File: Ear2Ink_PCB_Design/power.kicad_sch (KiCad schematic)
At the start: 20 parts, among them P1 OSTTE020104, U2 TPS562208DDCR, U3 AZ1117-3.3, U4 LM66100DCK, U5 LM66100DCK

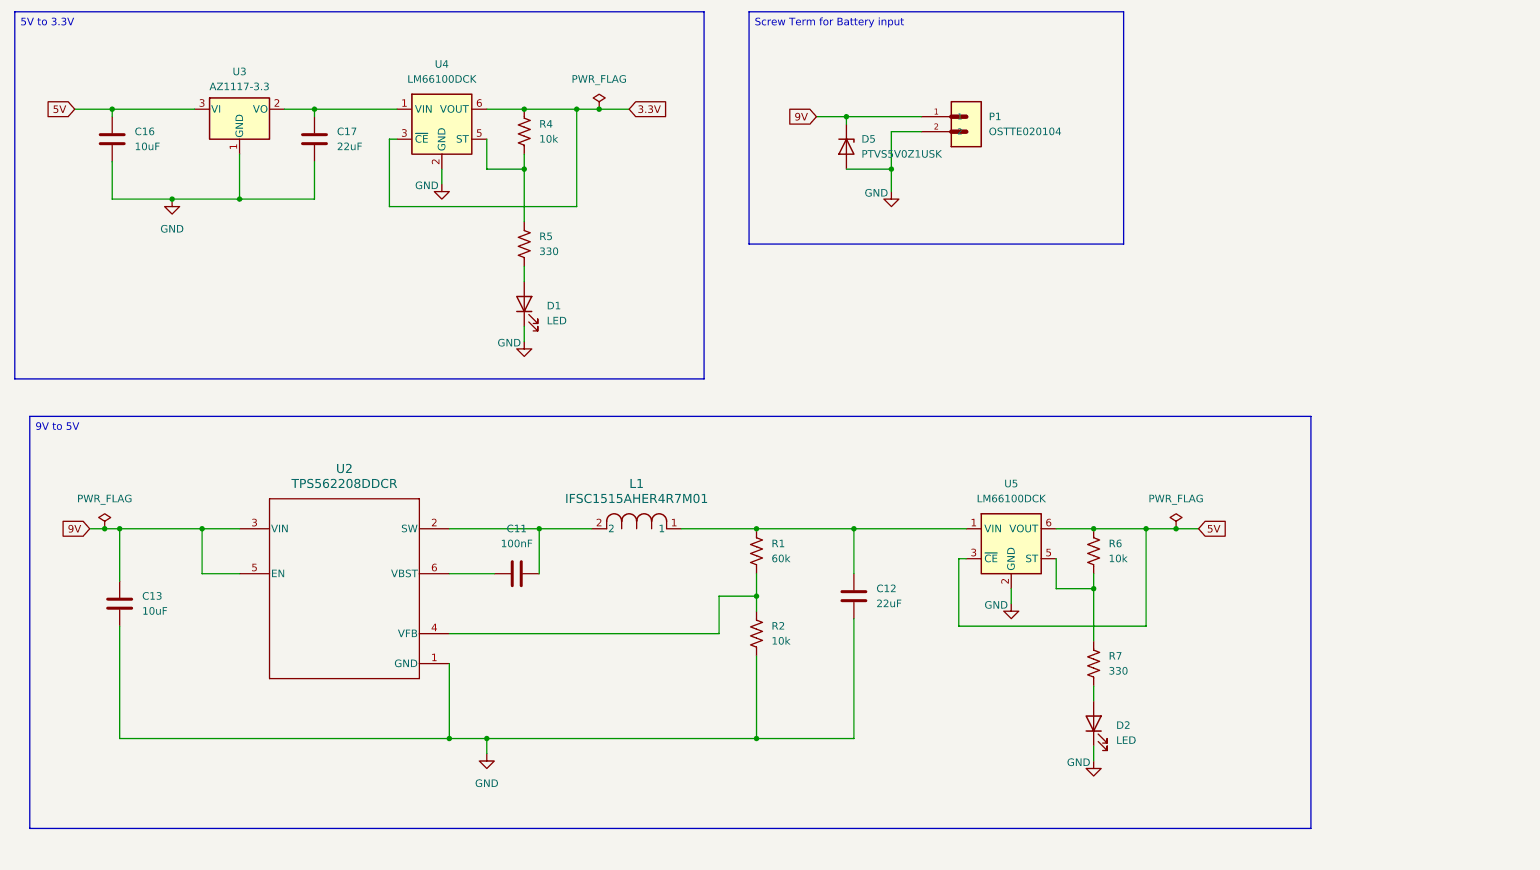
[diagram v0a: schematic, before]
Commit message: added current monitor
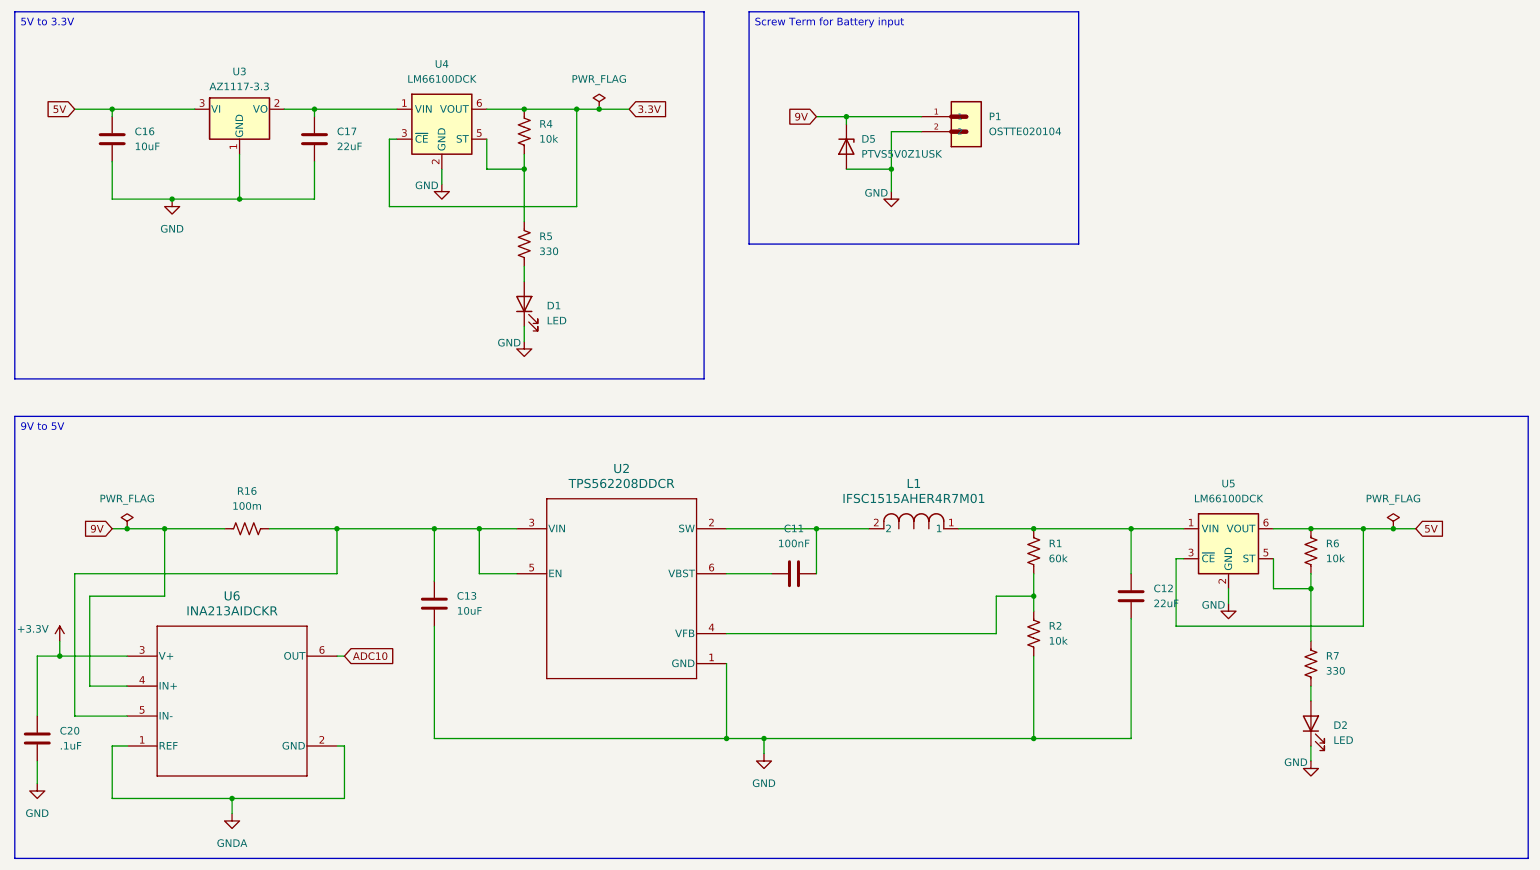
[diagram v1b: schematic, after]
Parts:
- added C20: .1uF, Capacitor_SMD:C_0603_1608Metric_Pad1.08x0.95mm_HandSolder, symbol Device:C
- added R16: 100m, Resistor_SMD:R_0603_1608Metric_Pad0.98x0.95mm_HandSolder, symbol Device:R_US
- added U6: INA213AIDCKR, Current_Monitor:DCK0006A_N, symbol Current_Monitor:INA213AIDCKR
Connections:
- net 9V: now also R16.2, U6.4 (IN+); no longer C13.2, U2.3 (VIN), U2.5 (EN)
- net GND: now also C20.1
- new net: C13.2, R16.1, U2.3 (VIN), U2.5 (EN), U6.5 (IN-)
- new net +3.3V: C20.2, U6.3 (V+)
- new net ADC10: U6.6 (OUT)
- new net GNDA: U6.1 (REF), U6.2 (GND)
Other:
- moved on the sheet: C11, C12, C13, D2, L1, R1, R2, R6, R7, U2, U5

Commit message: working on erc errors
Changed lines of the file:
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@@
 	)
 	(global_label "9V"
-		(shape input)
+		(shape output)
 		(at 158.75 40.64 180)
 		(fields_autoplaced yes)
@@
 	)
 	(global_label "5V"
-		(shape input)
+		(shape output)
 		(at 260.35 110.49 0)
 		(fields_autoplaced yes)
@@
 	)
 	(global_label "3.3V"
-		(shape input)
+		(shape output)
 		(at 127 39.37 0)
 		(fields_autoplaced yes)

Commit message: fixed erc stuff
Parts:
- added NT1: NetTie_2, NetTie:NetTie-2_SMD_Pad0.5mm, symbol Device:NetTie_2
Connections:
- net 3.3V is gone; now on net +3.3V: R4.1, U4.3 (~{CE}), U4.6 (VOUT)
- net GND: now also NT1.2
- net GNDA: now also NT1.1
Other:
- moved on the sheet: C11, R1

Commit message: SDIO to SPI
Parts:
- D1, D2: footprint Resistor_SMD:R_0805_2012Metric_Pad1.20x1.40mm_HandSolder -> LED_SMD:LED_0805_2012Metric_Pad1.15x1.40mm_HandSolder
- R1, R2, R4, R5, R6, R7: footprint Capacitor_SMD:C_0603_1608Metric_Pad1.08x0.95mm_HandSolder -> Resistor_SMD:R_0603_1608Metric_Pad0.98x0.95mm_HandSolder
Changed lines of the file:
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@@
 			)
 		)
-		(property "Footprint" "Capacitor_SMD:C_0603_1608Metric_Pad1.08x0.95mm_HandSolder"
+		(property "Footprint" "Resistor_SMD:R_0603_1608Metric_Pad0.98x0.95mm_HandSolder"
 			(at 243.586 114.554 90)
 			(effects
@@
 			)
 		)
-		(property "Footprint" "Capacitor_SMD:C_0603_1608Metric_Pad1.08x0.95mm_HandSolder"
+		(property "Footprint" "Resistor_SMD:R_0603_1608Metric_Pad0.98x0.95mm_HandSolder"
 			(at 196.596 115.824 90)
 			(effects
@@
 			)
 		)
-		(property "Footprint" "Capacitor_SMD:C_0603_1608Metric_Pad1.08x0.95mm_HandSolder"
+		(property "Footprint" "Resistor_SMD:R_0603_1608Metric_Pad0.98x0.95mm_HandSolder"
 			(at 243.586 133.604 90)
 			(effects
@@
 			)
 		)
-		(property "Footprint" "Resistor_SMD:R_0805_2012Metric_Pad1.20x1.40mm_HandSolder"
+		(property "Footprint" "LED_SMD:LED_0805_2012Metric_Pad1.15x1.40mm_HandSolder"
 			(at 109.22 72.39 0)
 			(effects
@@
 			)
 		)
-		(property "Footprint" "Capacitor_SMD:C_0603_1608Metric_Pad1.08x0.95mm_HandSolder"
+		(property "Footprint" "Resistor_SMD:R_0603_1608Metric_Pad0.98x0.95mm_HandSolder"
 			(at 110.236 43.434 90)
 			(effects
@@
 			)
 		)
-		(property "Footprint" "Resistor_SMD:R_0805_2012Metric_Pad1.20x1.40mm_HandSolder"
+		(property "Footprint" "LED_SMD:LED_0805_2012Metric_Pad1.15x1.40mm_HandSolder"
 			(at 242.57 143.51 0)
 			(effects
@@
 			)
 		)
-		(property "Footprint" "Capacitor_SMD:C_0603_1608Metric_Pad1.08x0.95mm_HandSolder"
+		(property "Footprint" "Resistor_SMD:R_0603_1608Metric_Pad0.98x0.95mm_HandSolder"
 			(at 196.596 128.524 90)
 			(effects
@@
 			)
 		)
-		(property "Footprint" "Capacitor_SMD:C_0603_1608Metric_Pad1.08x0.95mm_HandSolder"
+		(property "Footprint" "Resistor_SMD:R_0603_1608Metric_Pad0.98x0.95mm_HandSolder"
 			(at 110.236 62.484 90)
 			(effects

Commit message: resistors changed UPDATE LAYOUT
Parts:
- R5: value 330 -> 220
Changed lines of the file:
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@@
 			)
 		)
-		(property "Value" "330"
+		(property "Value" "220"
 			(at 111.76 63.4999 0)
 			(effects

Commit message: New Parts Added
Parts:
- L1: value IFSC1515AHER4R7M01 -> 47uH
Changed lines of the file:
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@@
 			)
 		)
-		(property "Value" "IFSC1515AHER4R7M01"
+		(property "Value" "47uH"
 			(at 175.26 105.41 0)
 			(effects

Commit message: Did a lot of stuff
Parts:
- added JP1: SolderJumper_2_Open, Jumper:SolderJumper-2_P1.3mm_Open_Pad1.0x1.5mm, symbol Jumper:SolderJumper_2_Open
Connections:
- net 9V: now also JP1.1 (A)
- net GND: now also U6.2 (GND)
- net GNDA: no longer U6.2 (GND)
- net Buck_In: now reaches C13.2, R16.1, U2.3 (VIN), U2.5 (EN), U6.5 (IN-)
- net Buck_In: now also JP1.2 (B)
- net 5V_Out: now reaches C12.1, L1.1, R1.1, U5.1 (VIN)
- net LDO_Out: now reaches C17.1, U3.2 (VO), U4.1 (VIN)
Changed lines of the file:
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@@
 	)
 	(junction
-		(at 59.69 156.21)
+		(at 53.34 110.49)
 		(diameter 0)
 		(color 0 0 0 0)
@@
 	)
 	(junction
+		(at 39.37 156.21)
+		(diameter 0)
+		(color 0 0 0 0)
+	)
+	(junction
+		(at 69.85 110.49)
+		(diameter 0)
+		(color 0 0 0 0)
+	)
+	(junction
 		(at 30.48 132.08)
 		(diameter 0)
@@
 	)
 	(junction
-		(at 50.8 156.21)
-		(diameter 0)
-		(color 0 0 0 0)
-	)
-	(junction
 		(at 154.94 110.49)
 		(diameter 0)
@@
 	(wire
 		(pts
+			(xy 58.42 100.33) (xy 53.34 100.33)
+		)
+		(stroke
+			(width 0)
+			(type default)
+		)
+	)
+	(wire
+		(pts
 			(xy 41.91 137.16) (xy 35.56 137.16)
 		)
@@
 	(wire
 		(pts
-			(xy 50.8 156.21) (xy 59.69 156.21)
-		)
-		(stroke
-			(width 0)
-			(type default)
-		)
-	)
-	(wire
-		(pts
 			(xy 189.23 128.27) (xy 189.23 121.92)
 		)
@@
 	(wire
 		(pts
-			(xy 39.37 156.21) (xy 50.8 156.21)
-		)
-		(stroke
-			(width 0)
-			(type default)
-		)
-	)
-	(wire
-		(pts
 			(xy 195.58 132.08) (xy 195.58 146.05)
 		)
@@
 	(wire
 		(pts
+			(xy 39.37 156.21) (xy 50.8 156.21)
+		)
+		(stroke
+			(width 0)
+			(type default)
+		)
+	)
+	(wire
+		(pts
 			(xy 73.66 39.37) (xy 87.63 39.37)
 		)
@@
 	(wire
 		(pts
+			(xy 69.85 110.49) (xy 73.66 110.49)
+		)
+		(stroke
+			(width 0)
+			(type default)
+		)
+	)
+	(wire
+		(pts
+			(xy 53.34 110.49) (xy 58.42 110.49)
+		)
+		(stroke
+			(width 0)
+			(type default)
+		)
+	)
+	(wire
+		(pts
 			(xy 242.57 120.65) (xy 236.22 120.65)
 		)
@@
 	(wire
 		(pts
-			(xy 66.04 110.49) (xy 73.66 110.49)
+			(xy 66.04 110.49) (xy 69.85 110.49)
 		)
 		(stroke
@@
 	(wire
 		(pts
+			(xy 69.85 100.33) (xy 69.85 110.49)
+		)
+		(stroke
+			(width 0)
+			(type default)
+		)
+	)
+	(wire
+		(pts
 			(xy 143.51 146.05) (xy 149.86 146.05)
 		)
@@
 	(wire
 		(pts
-			(xy 48.26 110.49) (xy 58.42 110.49)
+			(xy 48.26 110.49) (xy 53.34 110.49)
 		)
 		(stroke
@@
 	(wire
 		(pts
-			(xy 59.69 156.21) (xy 78.74 156.21)
+			(xy 236.22 120.65) (xy 236.22 115.57)
 		)
 		(stroke
@@
 	(wire
 		(pts
-			(xy 236.22 120.65) (xy 236.22 115.57)
+			(xy 39.37 39.37) (xy 53.34 39.37)
 		)
 		(stroke
@@
 	(wire
 		(pts
-			(xy 39.37 39.37) (xy 53.34 39.37)
+			(xy 53.34 100.33) (xy 53.34 110.49)
 		)
 		(stroke
@@
 	(wire
 		(pts
-			(xy 59.69 156.21) (xy 59.69 158.75)
+			(xy 39.37 156.21) (xy 39.37 158.75)
 		)
 		(stroke
@@
 	(wire
 		(pts
+			(xy 66.04 100.33) (xy 69.85 100.33)
+		)
+		(stroke
+			(width 0)
+			(type default)
+		)
+	)
+	(wire
+		(pts
 			(xy 242.57 120.65) (xy 242.57 129.54)
 		)
@@
 		)
 	)
+	(label "LDO_Out"
+		(at 76.2 39.37 0)
+		(effects
+			(font
+				(size 1.27 1.27)
+			)
+			(justify left bottom)
+		)
+	)
+	(label "5V_Out"
+		(at 186.69 110.49 0)
+		(effects
+			(font
+				(size 1.27 1.27)
+			)
+			(justify left bottom)
+		)
+	)
+	(label "Buck_In"
+		(at 86.36 110.49 0)
+		(effects
+			(font
+				(size 1.27 1.27)
+			)
+			(justify left bottom)
+		)
+	)
 	(global_label "9V"
 		(shape input)
@@
 	(symbol
 		(lib_id "power:GNDA")
-		(at 59.69 158.75 0)
+		(at 39.37 158.75 0)
 		(unit 1)
 		(exclude_from_sim no)
@@
 		(fields_autoplaced yes)
 		(property "Reference" "#PWR034"
-			(at 59.69 165.1 0)
+			(at 39.37 165.1 0)
 			(effects
 				(font
@@
 		)
 		(property "Value" "GNDA"
-			(at 59.69 163.83 0)
+			(at 39.37 163.83 0)
 			(effects
 				(font
@@
 		)
 		(property "Footprint" ""
-			(at 59.69 158.75 0)
+			(at 39.37 158.75 0)
 			(effects
 				(font
@@
 		)
 		(property "Datasheet" ""
-			(at 59.69 158.75 0)
+			(at 39.37 158.75 0)
 			(effects
 				(font
@@
 		)
 		(property "Description" "Power symbol creates a global label with name \"GNDA\" , analog ground"
-			(at 59.69 158.75 0)
+			(at 39.37 158.75 0)
 			(effects
 				(font
@@
 	)
 	(symbol
+		(lib_id "power:GND")
+		(at 78.74 156.21 0)
+		(unit 1)
+		(exclude_from_sim no)
+		(in_bom yes)
+		(on_board yes)
+		(dnp no)
+		(fields_autoplaced yes)
+		(property "Reference" "#PWR048"
+			(at 78.74 162.56 0)
+			(effects
+				(font
+					(size 1.27 1.27)
+				)
+				(hide yes)
+			)
+		)
+		(property "Value" "GND"
+			(at 78.74 161.29 0)
+			(effects
+				(font
+					(size 1.27 1.27)
+				)
+			)
+		)
+		(property "Footprint" ""
+			(at 78.74 156.21 0)
+			(effects
+				(font
+					(size 1.27 1.27)
+				)
+				(hide yes)
+			)
+		)
+		(property "Datasheet" ""
+			(at 78.74 156.21 0)
+			(effects
+				(font
+					(size 1.27 1.27)
+				)
+				(hide yes)
+			)
+		)
+		(property "Description" "Power symbol creates a global label with name \"GND\" , ground"
+			(at 78.74 156.21 0)
+			(effects
+				(font
+					(size 1.27 1.27)
+				)
+				(hide yes)
+			)
+		)
+		(pin "1"
+		)
+		(instances
+			(project "Ear2Ink_PCB_Design"
+				(path "/cdb6d8ac-bdfd-4608-bf70-aa82e76498ad/f1b1c289-1e04-4344-a520-d726c8046e56"
+					(reference "#PWR048")
+					(unit 1)
+				)
+			)
+		)
+	)
+	(symbol
 		(lib_id "power:+3.3V")
 		(at 121.92 39.37 0)
@@
 					(unit 1)
 				)
+			)
+		)
+	)
+	(symbol
+		(lib_id "Jumper:SolderJumper_2_Open")
+		(at 62.23 100.33 0)
+		(unit 1)
+		(exclude_from_sim no)
+		(in_bom no)
+		(on_board yes)
+		(dnp no)
+		(fields_autoplaced yes)
+		(property "Reference" "JP1"
+			(at 62.23 93.98 0)
+			(effects
+				(font
+					(size 1.27 1.27)
+				)
+			)
+		)
+		(property "Value" "SolderJumper_2_Open"
+			(at 62.23 96.52 0)
+			(effects
+				(font
+					(size 1.27 1.27)
+				)
+			)
+		)
+		(property "Footprint" "Jumper:SolderJumper-2_P1.3mm_Open_Pad1.0x1.5mm"
+			(at 62.23 100.33 0)
+			(effects
+				(font
+					(size 1.27 1.27)
+				)
+				(hide yes)
+			)
+		)
+		(property "Datasheet" "~"
+			(at 62.23 100.33 0)
+			(effects
+				(font
+					(size 1.27 1.27)
+				)
+				(hide yes)
+			)
+		)
+		(property "Description" "Solder Jumper, 2-pole, open"
+			(at 62.23 100.33 0)
+			(effects
+				(font
+					(size 1.27 1.27)
+				)
+				(hide yes)
+			)
+		)
+		(pin "2"
+		)
+		(pin "1"
+		)
+		(instances
+			(project ""
+				(path "/cdb6d8ac-bdfd-4608-bf70-aa82e76498ad/f1b1c289-1e04-4344-a520-d726c8046e56"
+					(reference "JP1")
+					(unit 1)
+				)

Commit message: done
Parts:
- removed D1: LED, LED_SMD:LED_0805_2012Metric_Pad1.15x1.40mm_HandSolder, symbol Device:LED
- removed D5: PTVS5V0Z1USK, Diode_SMD:Nexperia_DSN1608-2_1.6x0.8mm, symbol Diode:PTVS5V0Z1USK
- removed R4: 10k, Resistor_SMD:R_0603_1608Metric_Pad0.98x0.95mm_HandSolder, symbol Device:R_US
- removed R5: 220, Resistor_SMD:R_0603_1608Metric_Pad0.98x0.95mm_HandSolder, symbol Device:R_US
- removed U4: LM66100DCK, Package_TO_SOT_SMD:SOT-363_SC-70-6, symbol Power_Management:LM66100DCK
- added C7: .1uF, Capacitor_SMD:C_0603_1608Metric_Pad1.08x0.95mm_HandSolder, symbol Device:C
- added D15, D16, D17: LED, LED_SMD:LED_0805_2012Metric_Pad1.15x1.40mm_HandSolder, symbol Device:LED
- added H1, H2, H3, H4: MountingHole, MountingHole:MountingHole_2.5mm, symbol Mechanical:MountingHole
- added R23: 690, Resistor_SMD:R_0603_1608Metric_Pad0.98x0.95mm_HandSolder, symbol Device:R_US
- added R24: 330, Resistor_SMD:R_0603_1608Metric_Pad0.98x0.95mm_HandSolder, symbol Device:R_US
- added R25: 120, Resistor_SMD:R_0603_1608Metric_Pad0.98x0.95mm_HandSolder, symbol Device:R_US
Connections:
- net LDO_Out is gone; now on net +3.3V: C17.1, U3.2 (VO)
- net +3.3V: now also R25.1
- net 5V_Out: now also R24.1
- net 9V: now also C7.2, R23.1
- net GND: now also C7.1, D15.1 (K), D16.1 (K), D17.1 (K)
- new net: D17.2 (A), R25.2
- new net: D15.2 (A), R23.2
- new net: D16.2 (A), R24.2
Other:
- moved on the sheet: C12, C17, D2, P1, R6, R7, U5
